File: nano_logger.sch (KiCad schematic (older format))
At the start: 17 parts, among them CON1 AVR-ISP-6, IC1 ATMEGA328P-M, P1 SDMICRO, P2 P1, P3 FTDI, Y1 RESONATORSMD

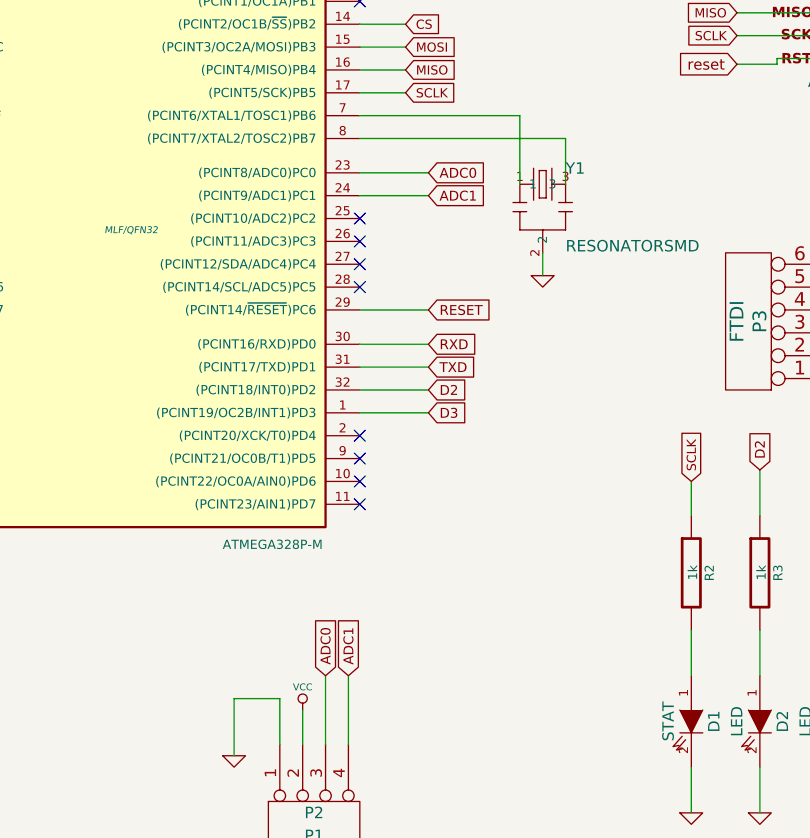
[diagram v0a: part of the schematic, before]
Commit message: Moved parts around and routed
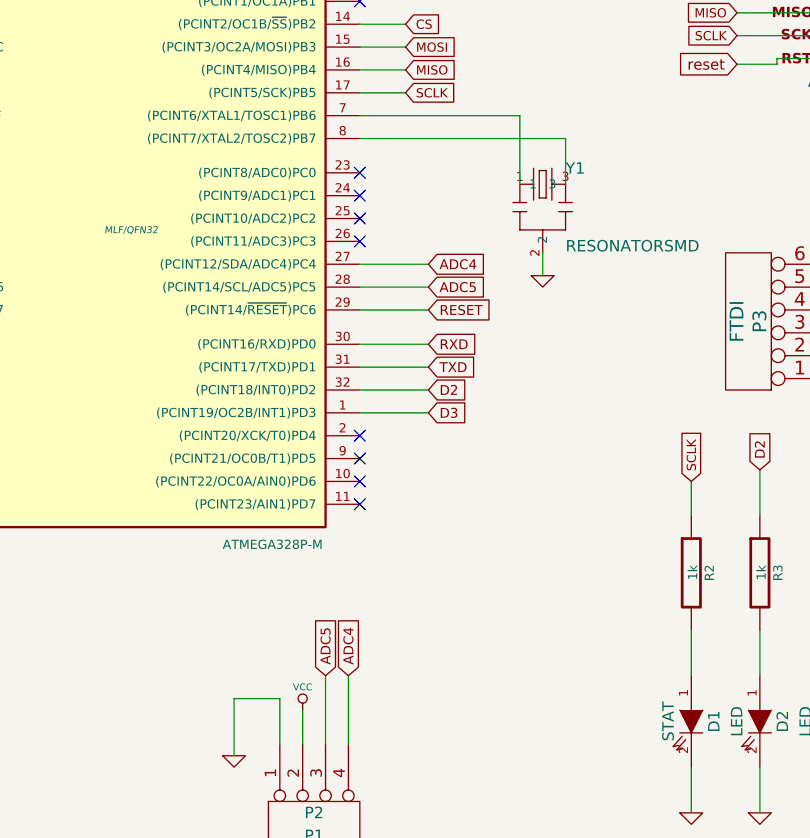
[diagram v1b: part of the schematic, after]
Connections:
- net ADC4: now reaches IC1.27 ((PCINT12/SDA/ADC4)PC4)
- net ADC4: now also P2.4 (P4)
- net ADC5: now reaches IC1.28 ((PCINT14/SCL/ADC5)PC5)
- net ADC5: now also P2.3 (P3)
- net ADC0: no longer names the net of IC1.23 ((PCINT8/ADC0)PC0)
- net ADC0: no longer P2.3 (P3)
- net ADC1: no longer names the net of IC1.24 ((PCINT9/ADC1)PC1)
- net ADC1: no longer P2.4 (P4)
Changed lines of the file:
@@
 Wire Wire Line
 	5600 5200 5600 5350
-Text GLabel 6150 2850 2    43   Input ~ 0
-ADC0
-Text GLabel 6150 2950 2    43   Input ~ 0
-ADC1
+Text GLabel 5800 5050 1    43   Input ~ 0
+ADC4
 Text GLabel 5700 5050 1    43   Input ~ 0
-ADC0
-Text GLabel 5800 5050 1    43   Input ~ 0
-ADC1
+ADC5
 Wire Wire Line
 	5700 5050 5700 5350
 Wire Wire Line
 	5800 5050 5800 5350
-Wire Wire Line
-	6150 2850 5850 2850
-Wire Wire Line
-	6150 2950 5850 2950
 $Comp
 L C C1
@@
 NoConn ~ 5850 4100
 NoConn ~ 5850 4000
-NoConn ~ 5850 3350
-NoConn ~ 5850 3250
 NoConn ~ 5850 3150
 NoConn ~ 5850 3050
+Text GLabel 6150 3250 2    43   Input ~ 0
+ADC4
+Text GLabel 6150 3350 2    43   Input ~ 0
+ADC5
+Wire Wire Line
+	5850 3250 6150 3250
+Wire Wire Line
+	5850 3350 6150 3350
+NoConn ~ 5850 2850
+NoConn ~ 5850 2950
 $EndSCHEMATC
